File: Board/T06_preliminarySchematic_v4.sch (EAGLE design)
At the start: 57 parts, among them M1 SSW-102-02-S-S, M2 SSW-102-02-S-S, Q3 2n3904, U1 ATMEGA328P_PDIP, X1 SSW-105-02-S-S, X2 SSW-102-02-S-S

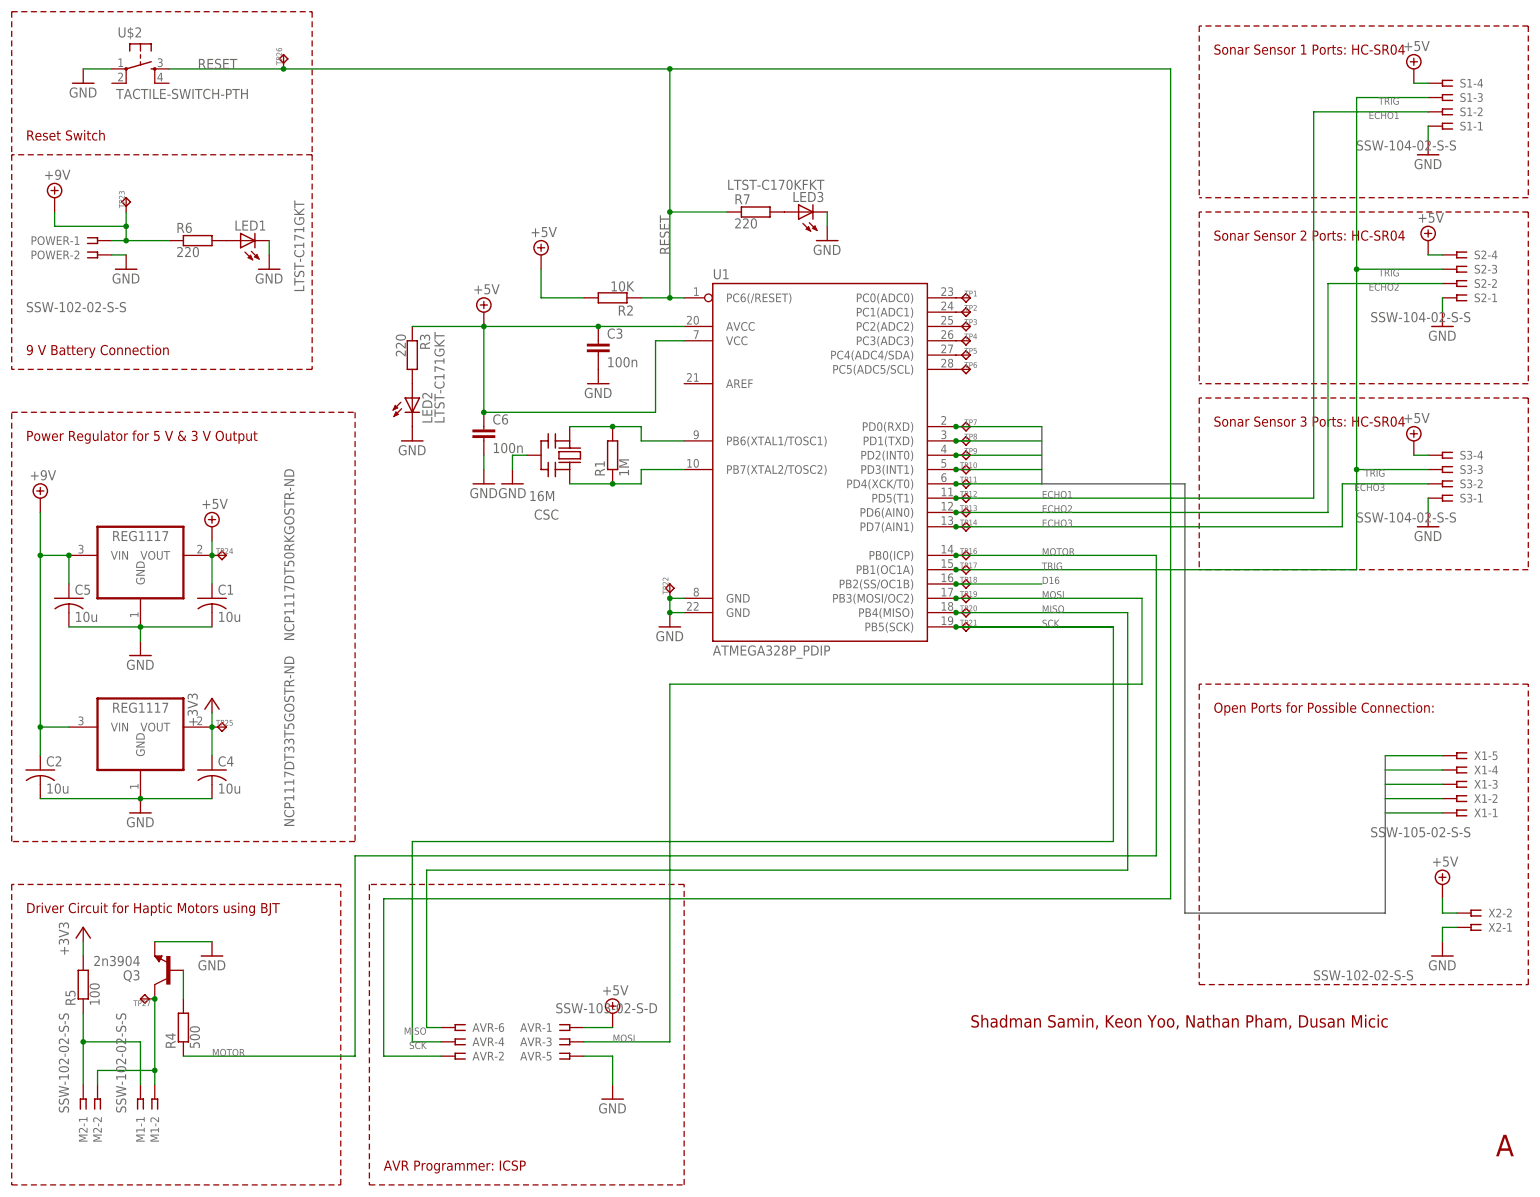
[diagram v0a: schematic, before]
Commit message: Built the prototype. The sensor doesnt allow us the trigger all the sensors in parallel. So we are using individual pins to trigger the sensors. That is reflected in this revision
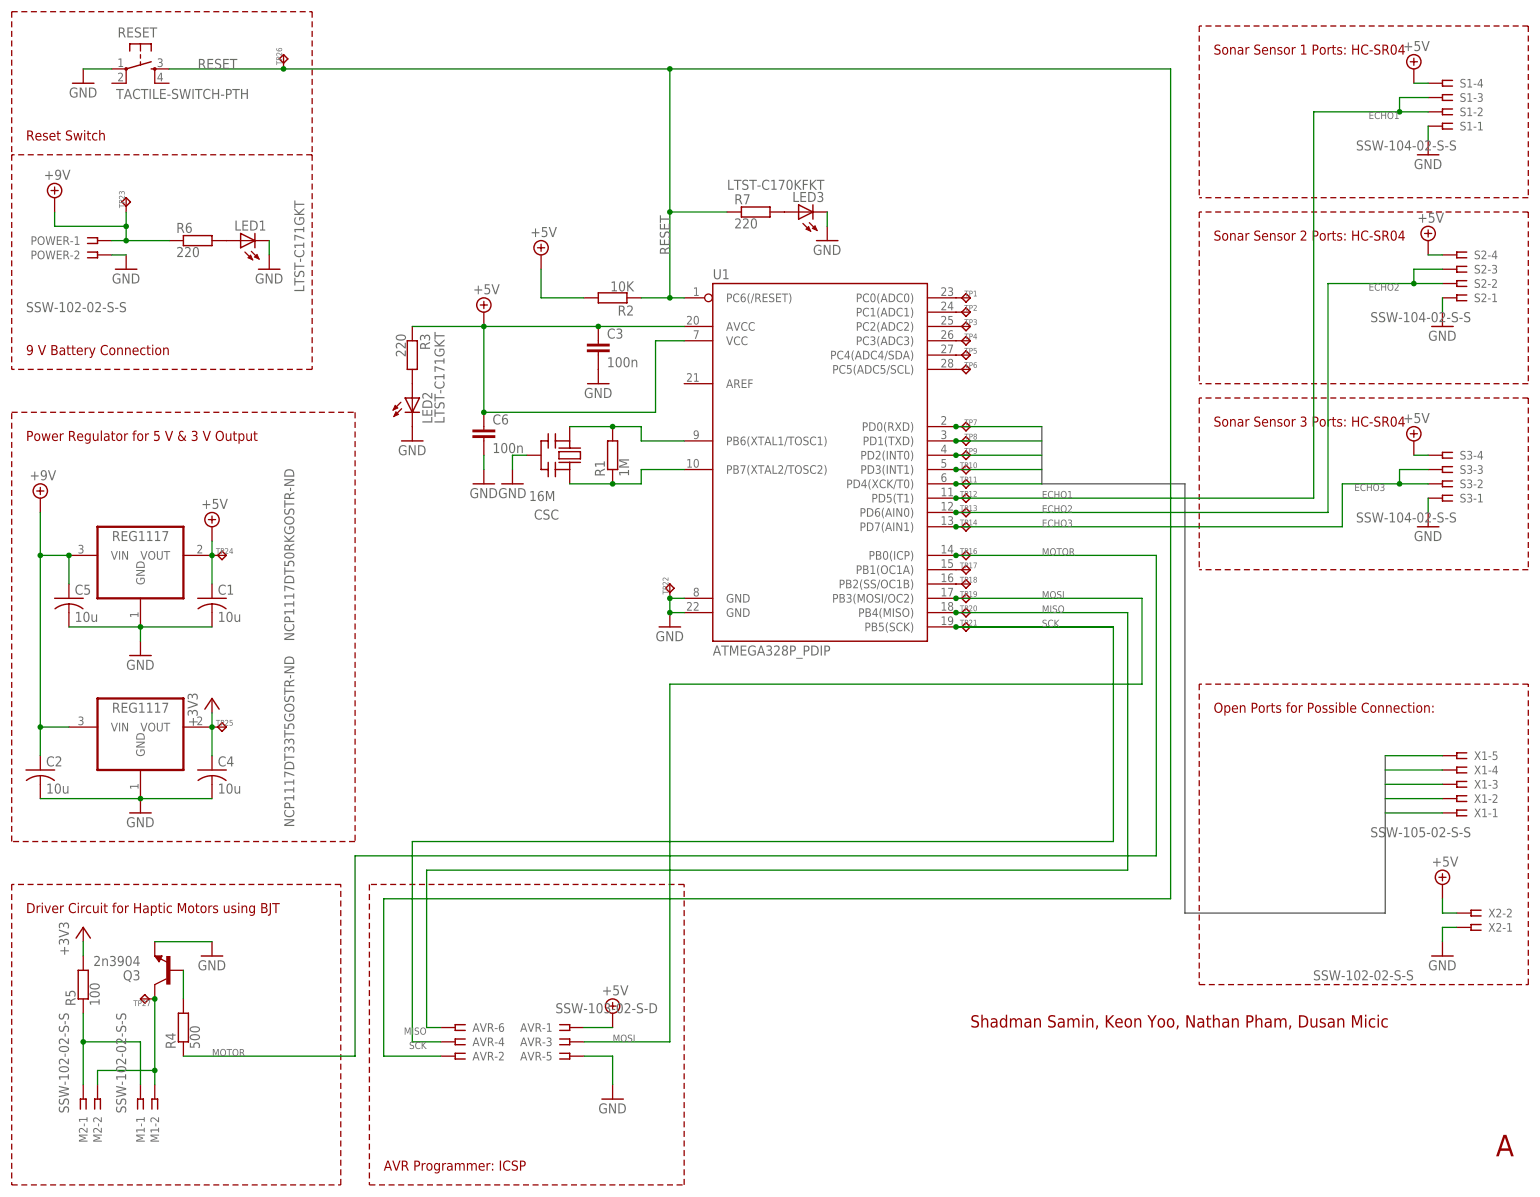
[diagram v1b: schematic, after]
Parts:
- renumbered U$2 to RESET
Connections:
- removed net TRIG: S1-3.1, S2-3.1, S3-3.1, TP17.TP, U1.PB1(OC1A)
- new net N$15: TP17.TP, U1.PB1(OC1A)
- net ECHO1: now also S1-3.1
- net ECHO2: now also S2-3.1
- net ECHO3: now also S3-3.1
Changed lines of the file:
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@@
 <?xml version="1.0" encoding="utf-8"?>
 <!DOCTYPE eagle SYSTEM "eagle.dtd">
-<eagle version="7.4.0">
+<eagle version="7.3.0">
 <drawing>
 <settings>
@@
 <part name="R2" library="eagle-ltspice" deviceset="R" device="R0603" value="10K"/>
 <part name="GND2" library="supply1" deviceset="GND" device=""/>
-<part name="U$2" library="GeekAmmo" deviceset="TACTILE-SWITCH" device="-PTH"/>
+<part name="RESET" library="GeekAmmo" deviceset="TACTILE-SWITCH" device="-PTH"/>
 <part name="S1" library="con-samtec" deviceset="SSW-104-02-S-S" device=""/>
 <part name="NCP1117DT50RKGOSTR-ND" library="burr-brown" deviceset="REG1117" device="" value="REG1117"/>
@@
 <attribute name="VALUE" x="12.7" y="20.32" size="1.778" layer="96"/>
 </instance>
-<instance part="U$2" gate="G$1" x="-78.74" y="121.92" smashed="yes">
+<instance part="RESET" gate="G$1" x="-78.74" y="121.92" smashed="yes">
 <attribute name="NAME" x="-82.804" y="127.508" size="1.778" layer="95"/>
 <attribute name="VALUE" x="-83.058" y="116.586" size="1.778" layer="96"/>
@@
 <segment>
 <label x="-68.58" y="121.92" size="1.778" layer="150"/>
-<pinref part="U$2" gate="G$1" pin="3"/>
+<pinref part="RESET" gate="G$1" pin="3"/>
 <pinref part="R2" gate="G$1" pin="1"/>
 <pinref part="U1" gate="G$1" pin="PC6(/RESET)"/>
@@
 </segment>
 <segment>
-<pinref part="U$2" gate="G$1" pin="1"/>
+<pinref part="RESET" gate="G$1" pin="1"/>
 <wire x1="-83.82" y1="121.92" x2="-88.9" y2="121.92" width="0.1524" layer="91"/>
 <pinref part="GND6" gate="1" pin="GND"/>
@@
 <wire x1="-71.12" y1="-38.1" x2="-71.12" y2="-43.18" width="0.1524" layer="91"/>
 <pinref part="R4" gate="G$1" pin="2"/>
-</segment>
-</net>
-<net name="TRIG" class="0">
-<segment>
-<pinref part="S1" gate="-3" pin="1"/>
-<label x="144.78" y="116.84" size="1.27" layer="150" rot="R180"/>
-<pinref part="S2" gate="-3" pin="1"/>
-<label x="144.78" y="86.36" size="1.27" layer="150" rot="R180"/>
-<pinref part="U1" gate="G$1" pin="PB1(OC1A)"/>
-<label x="81.28" y="33.02" size="1.27" layer="150"/>
-<wire x1="66.04" y1="33.02" x2="137.16" y2="33.02" width="0.1524" layer="91"/>
-<wire x1="137.16" y1="33.02" x2="137.16" y2="50.8" width="0.1524" layer="91"/>
-<pinref part="S3" gate="-3" pin="1"/>
-<wire x1="149.86" y1="50.8" x2="137.16" y2="50.8" width="0.1524" layer="91"/>
-<label x="142.24" y="50.8" size="1.27" layer="150" rot="R180"/>
-<wire x1="152.4" y1="86.36" x2="137.16" y2="86.36" width="0.1524" layer="91"/>
-<wire x1="137.16" y1="86.36" x2="137.16" y2="50.8" width="0.1524" layer="91"/>
-<junction x="137.16" y="50.8"/>
-<wire x1="149.86" y1="116.84" x2="137.16" y2="116.84" width="0.1524" layer="91"/>
-<wire x1="137.16" y1="116.84" x2="137.16" y2="86.36" width="0.1524" layer="91"/>
-<junction x="137.16" y="86.36"/>
-<pinref part="TP17" gate="G$1" pin="TP"/>
-<junction x="66.04" y="33.02"/>
 </segment>
 </net>
@@
 <segment>
 <pinref part="U1" gate="G$1" pin="PB2(SS/OC1B)"/>
-<wire x1="81.28" y1="30.48" x2="66.04" y2="30.48" width="0.1524" layer="91"/>
-<label x="81.28" y="30.48" size="1.27" layer="150"/>
 <pinref part="TP18" gate="G$1" pin="TP"/>
-<junction x="66.04" y="30.48"/>
 </segment>
 </net>
@@
 <pinref part="S1" gate="-2" pin="1"/>
 <label x="144.78" y="114.3" size="1.27" layer="150" rot="R180"/>
-<wire x1="129.54" y1="114.3" x2="149.86" y2="114.3" width="0.1524" layer="91"/>
+<wire x1="129.54" y1="114.3" x2="144.78" y2="114.3" width="0.1524" layer="91"/>
 <pinref part="TP12" gate="G$1" pin="TP"/>
 <junction x="66.04" y="45.72"/>
+<pinref part="S1" gate="-3" pin="1"/>
+<wire x1="144.78" y1="114.3" x2="149.86" y2="114.3" width="0.1524" layer="91"/>
+<wire x1="149.86" y1="116.84" x2="144.78" y2="116.84" width="0.1524" layer="91"/>
+<wire x1="144.78" y1="116.84" x2="144.78" y2="114.3" width="0.1524" layer="91"/>
+<junction x="144.78" y="114.3"/>
 </segment>
 </net>
@@
 <pinref part="S2" gate="-2" pin="1"/>
 <label x="144.78" y="83.82" size="1.27" layer="150" rot="R180"/>
-<wire x1="132.08" y1="83.82" x2="152.4" y2="83.82" width="0.1524" layer="91"/>
+<wire x1="132.08" y1="83.82" x2="147.32" y2="83.82" width="0.1524" layer="91"/>
 <pinref part="TP13" gate="G$1" pin="TP"/>
 <junction x="66.04" y="43.18"/>
+<wire x1="147.32" y1="83.82" x2="152.4" y2="83.82" width="0.1524" layer="91"/>
+<wire x1="147.32" y1="83.82" x2="147.32" y2="86.36" width="0.1524" layer="91"/>
+<junction x="147.32" y="83.82"/>
+<pinref part="S2" gate="-3" pin="1"/>
+<wire x1="147.32" y1="86.36" x2="152.4" y2="86.36" width="0.1524" layer="91"/>
 </segment>
 </net>
@@
 <pinref part="S3" gate="-2" pin="1"/>
 <label x="142.24" y="48.26" size="1.27" layer="150" rot="R180"/>
-<wire x1="134.62" y1="48.26" x2="149.86" y2="48.26" width="0.1524" layer="91"/>
+<wire x1="134.62" y1="48.26" x2="144.78" y2="48.26" width="0.1524" layer="91"/>
 <pinref part="TP14" gate="G$1" pin="TP"/>
 <junction x="66.04" y="40.64"/>
+<wire x1="144.78" y1="48.26" x2="149.86" y2="48.26" width="0.1524" layer="91"/>
+<wire x1="144.78" y1="48.26" x2="144.78" y2="50.8" width="0.1524" layer="91"/>
+<junction x="144.78" y="48.26"/>
+<pinref part="S3" gate="-3" pin="1"/>
+<wire x1="144.78" y1="50.8" x2="149.86" y2="50.8" width="0.1524" layer="91"/>
 </segment>
 </net>
@@
 </segment>
 </net>
+<net name="N$15" class="0">
+<segment>
+<pinref part="U1" gate="G$1" pin="PB1(OC1A)"/>
+<pinref part="TP17" gate="G$1" pin="TP"/>
+</segment>
+</net>

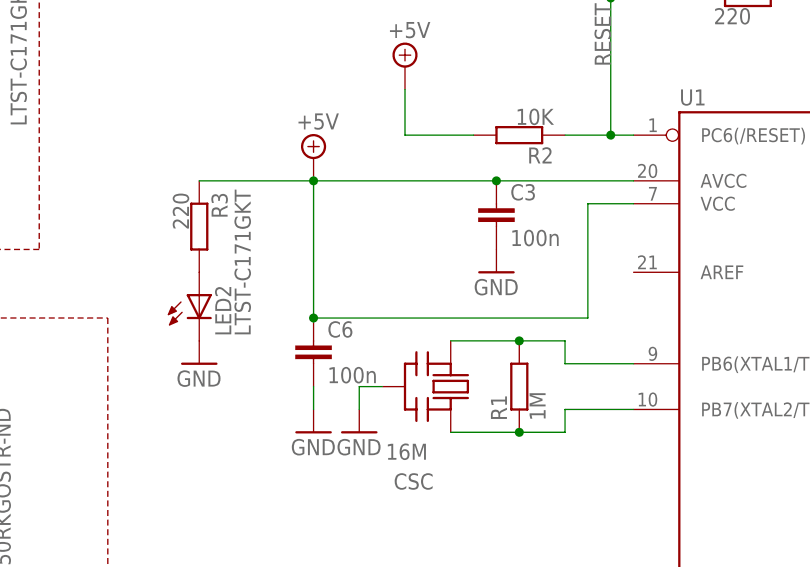
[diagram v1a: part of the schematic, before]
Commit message: Made changes to the cap size from 1005 to 0805
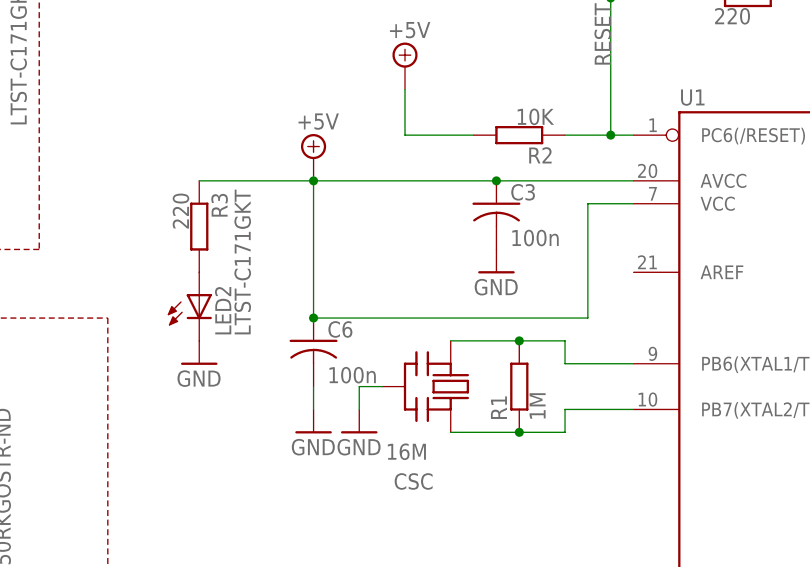
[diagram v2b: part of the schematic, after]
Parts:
- C3, C6: device eagle-ltspice:CC1005 -> rcl:C-USC0805K
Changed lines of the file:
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@@
 <grid distance="0.1" unitdist="inch" unit="inch" style="lines" multiple="1" display="no" altdistance="0.01" altunitdist="inch" altunit="inch"/>
 <layers>
-<layer number="1" name="Top" color="4" fill="1" visible="no" active="no"/>
-<layer number="16" name="Bottom" color="1" fill="1" visible="no" active="no"/>
-<layer number="17" name="Pads" color="2" fill="1" visible="no" active="no"/>
-<layer number="18" name="Vias" color="2" fill="1" visible="no" active="no"/>
-<layer number="19" name="Unrouted" color="6" fill="1" visible="no" active="no"/>
-<layer number="20" name="Dimension" color="15" fill="1" visible="no" active="no"/>
-<layer number="21" name="tPlace" color="7" fill="1" visible="no" active="no"/>
-<layer number="22" name="bPlace" color="7" fill="1" visible="no" active="no"/>
-<layer number="23" name="tOrigins" color="15" fill="1" visible="no" active="no"/>
-<layer number="24" name="bOrigins" color="15" fill="1" visible="no" active="no"/>
-<layer number="25" name="tNames" color="7" fill="1" visible="no" active="no"/>
-<layer number="26" name="bNames" color="7" fill="1" visible="no" active="no"/>
-<layer number="27" name="tValues" color="7" fill="1" visible="no" active="no"/>
-<layer number="28" name="bValues" color="7" fill="1" visible="no" active="no"/>
+<layer number="1" name="Top" color="4" fill="1" visible="yes" active="no"/>
+<layer number="16" name="Bottom" color="1" fill="1" visible="yes" active="no"/>
+<layer number="17" name="Pads" color="2" fill="1" visible="yes" active="no"/>
+<layer number="18" name="Vias" color="2" fill="1" visible="yes" active="no"/>
+<layer number="19" name="Unrouted" color="6" fill="1" visible="yes" active="no"/>
+<layer number="20" name="Dimension" color="15" fill="1" visible="yes" active="no"/>
+<layer number="21" name="tPlace" color="7" fill="1" visible="yes" active="no"/>
+<layer number="22" name="bPlace" color="7" fill="1" visible="yes" active="no"/>
+<layer number="23" name="tOrigins" color="15" fill="1" visible="yes" active="no"/>
+<layer number="24" name="bOrigins" color="15" fill="1" visible="yes" active="no"/>
+<layer number="25" name="tNames" color="7" fill="1" visible="yes" active="no"/>
+<layer number="26" name="bNames" color="7" fill="1" visible="yes" active="no"/>
+<layer number="27" name="tValues" color="7" fill="1" visible="yes" active="no"/>
+<layer number="28" name="bValues" color="7" fill="1" visible="yes" active="no"/>
 <layer number="29" name="tStop" color="7" fill="3" visible="no" active="no"/>
 <layer number="30" name="bStop" color="7" fill="6" visible="no" active="no"/>
@@
 <layer number="35" name="tGlue" color="7" fill="4" visible="no" active="no"/>
 <layer number="36" name="bGlue" color="7" fill="5" visible="no" active="no"/>
-<layer number="37" name="tTest" color="7" fill="1" visible="no" active="no"/>
-<layer number="38" name="bTest" color="7" fill="1" visible="no" active="no"/>
+<layer number="37" name="tTest" color="7" fill="1" visible="yes" active="no"/>
+<layer number="38" name="bTest" color="7" fill="1" visible="yes" active="no"/>
 <layer number="39" name="tKeepout" color="4" fill="11" visible="no" active="no"/>
 <layer number="40" name="bKeepout" color="1" fill="11" visible="no" active="no"/>
@@
 <layer number="44" name="Drills" color="7" fill="1" visible="no" active="no"/>
 <layer number="45" name="Holes" color="7" fill="1" visible="no" active="no"/>
-<layer number="46" name="Milling" color="3" fill="1" visible="no" active="no"/>
-<layer number="47" name="Measures" color="7" fill="1" visible="no" active="no"/>
-<layer number="48" name="Document" color="7" fill="1" visible="no" active="no"/>
-<layer number="49" name="Reference" color="7" fill="1" visible="no" active="no"/>
-<layer number="50" name="dxf" color="7" fill="1" visible="no" active="no"/>
-<layer number="51" name="tDocu" color="7" fill="1" visible="no" active="no"/>
-<layer number="52" name="bDocu" color="7" fill="1" visible="no" active="no"/>
-<layer number="53" name="tGND_GNDA" color="7" fill="9" visible="no" active="no"/>
-<layer number="54" name="bGND_GNDA" color="1" fill="9" visible="no" active="no"/>
-<layer number="56" name="wert" color="7" fill="1" visible="no" active="no"/>
-<layer number="57" name="tCAD" color="7" fill="1" visible="no" active="no"/>
-<layer number="59" name="tCarbon" color="7" fill="1" visible="no" active="no"/>
-<layer number="60" name="bCarbon" color="7" fill="1" visible="no" active="no"/>
+<layer number="46" name="Milling" color="3" fill="1" visible="yes" active="no"/>
+<layer number="47" name="Measures" color="7" fill="1" visible="yes" active="no"/>
+<layer number="48" name="Document" color="7" fill="1" visible="yes" active="no"/>
+<layer number="49" name="Reference" color="7" fill="1" visible="yes" active="no"/>
+<layer number="50" name="dxf" color="7" fill="1" visible="yes" active="no"/>
+<layer number="51" name="tDocu" color="7" fill="1" visible="yes" active="no"/>
+<layer number="52" name="bDocu" color="7" fill="1" visible="yes" active="no"/>
+<layer number="53" name="tGND_GNDA" color="7" fill="9" visible="yes" active="no"/>
+<layer number="54" name="bGND_GNDA" color="1" fill="9" visible="yes" active="no"/>
+<layer number="56" name="wert" color="7" fill="1" visible="yes" active="no"/>
+<layer number="57" name="tCAD" color="7" fill="1" visible="yes" active="no"/>
+<layer number="59" name="tCarbon" color="7" fill="1" visible="yes" active="no"/>
+<layer number="60" name="bCarbon" color="7" fill="1" visible="yes" active="no"/>
 <layer number="90" name="Modules" color="5" fill="1" visible="yes" active="yes"/>
 <layer number="91" name="Nets" color="2" fill="1" visible="yes" active="yes"/>
@@
 <part name="GND9" library="supply1" deviceset="GND" device=""/>
 <part name="GND12" library="supply1" deviceset="GND" device=""/>
-<part name="C3" library="eagle-ltspice" deviceset="C" device="C1005" value="100n"/>
+<part name="C3" library="rcl" deviceset="C-US" device="C0805K" value="100n"/>
 <part name="AVR" library="con-samtec" deviceset="SSW-103-02-S-D" device=""/>
 <part name="SUPPLY1" library="supply2" deviceset="+9V" device=""/>
@@
 <part name="GND14" library="supply1" deviceset="GND" device=""/>
 <part name="SUPPLY10" library="supply2" deviceset="+5V" device=""/>
-<part name="C6" library="eagle-ltspice" deviceset="C" device="C1005" value="100n"/>
+<part name="C6" library="rcl" deviceset="C-US" device="C0805K" value="100n"/>
 <part name="GND15" library="supply1" deviceset="GND" device=""/>
 <part name="GND16" library="supply1" deviceset="GND" device=""/>
